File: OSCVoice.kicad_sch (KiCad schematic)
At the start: 39 parts, among them U10 TL072, U5 MCP6004, U6 4066, U8 4066, U9 SSI2131

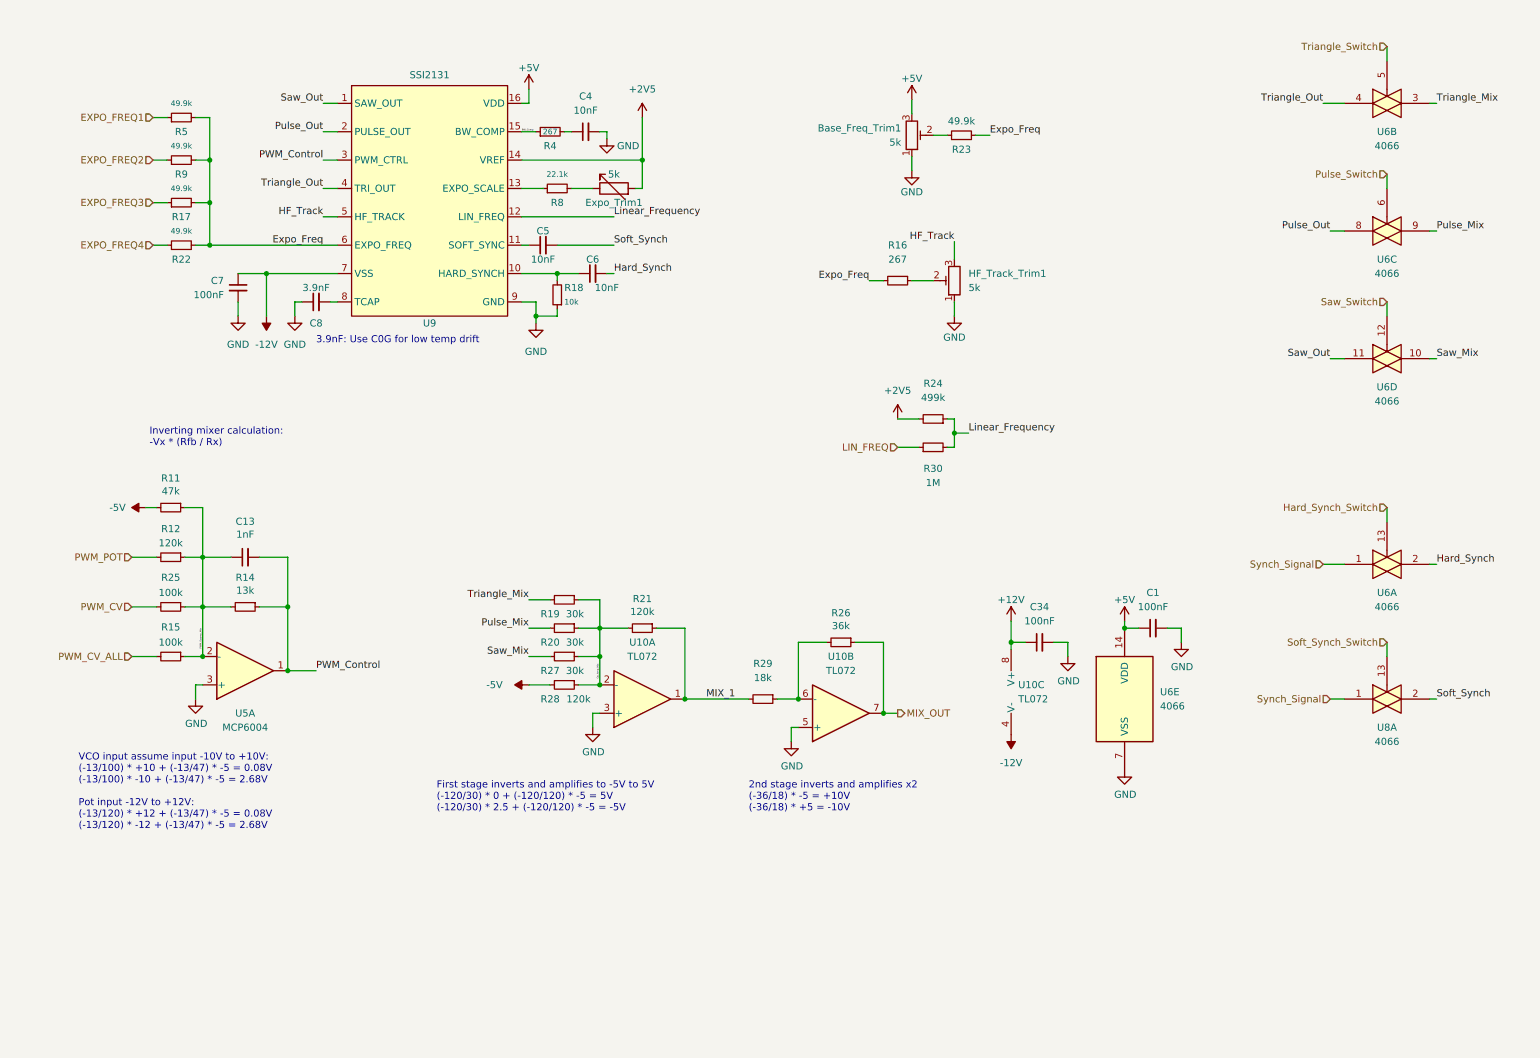
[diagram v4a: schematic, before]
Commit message: Duplicated layout of voices; power supply
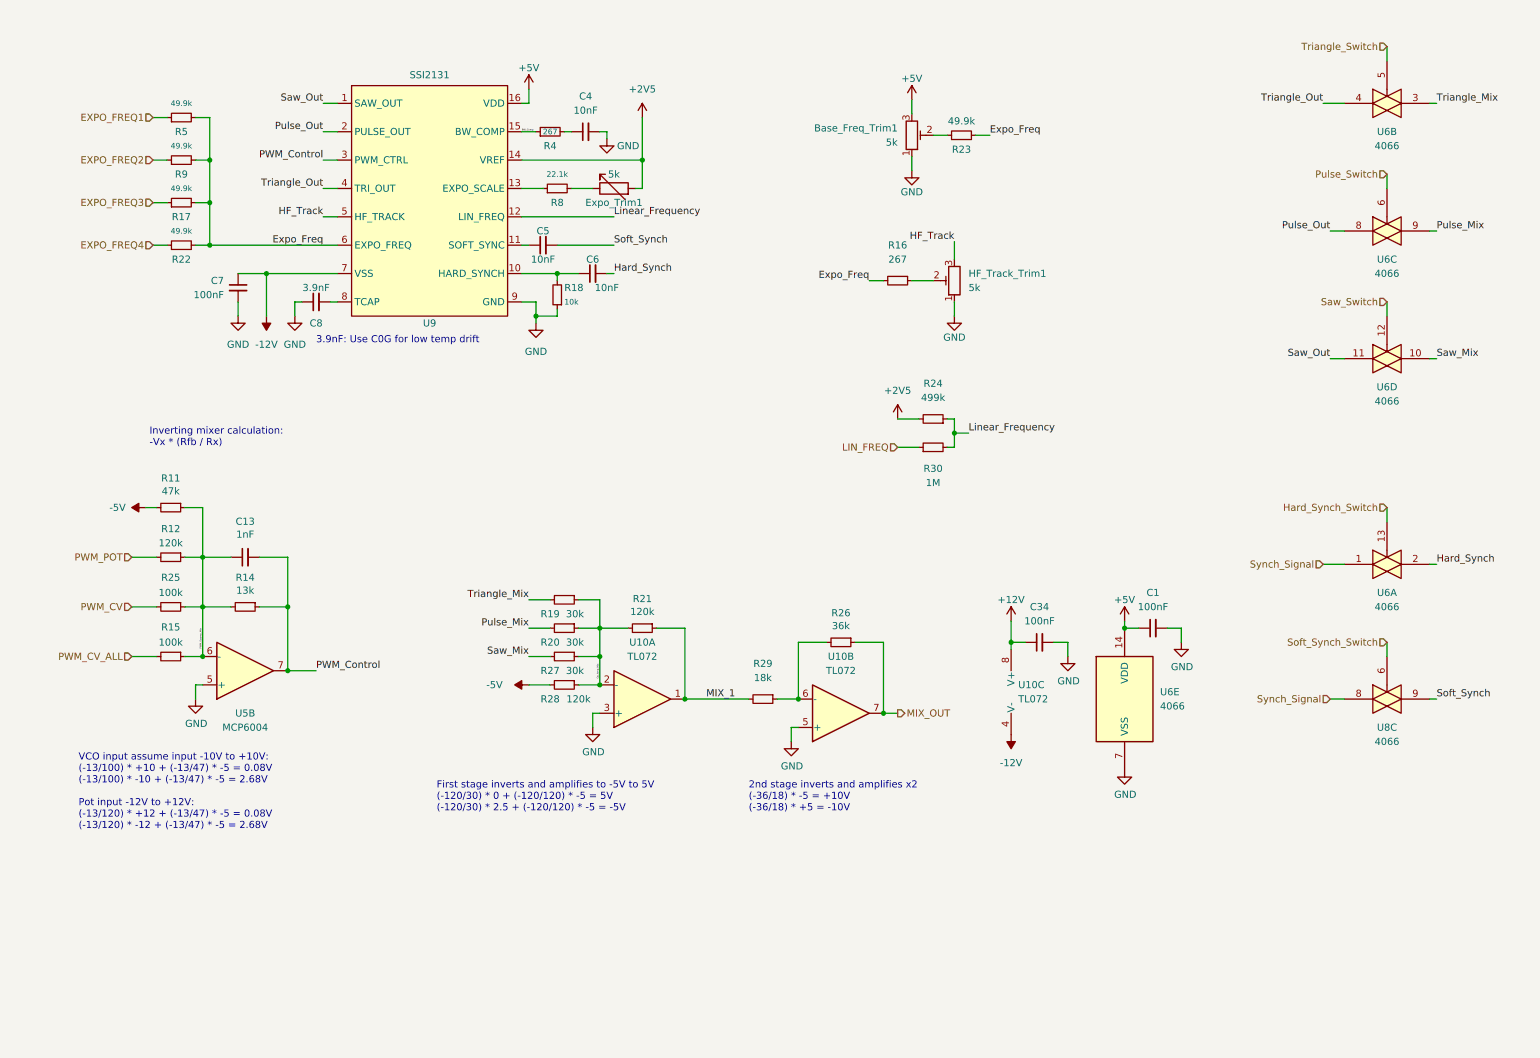
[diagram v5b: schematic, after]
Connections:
- net GND: now also U5.5 (+); no longer U5.3 (+)
- net PWM_Control: now also U5.7; no longer U5.1
- net PWM_Opamp_Mix: now also U5.6 (-); no longer U5.2 (-)
- net Soft_Synch: now also U8.9; no longer U8.2
- net Soft_Synch_Switch: now also U8.6; no longer U8.13
- net Synch_Signal: now also U8.8; no longer U8.1
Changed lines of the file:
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@@
     (pin "1")
   )
-  (symbol (lib_id "Amplifier_Operational:MCP6004") (at 54.61 130.81 0) (mirror x) (unit 1)
+  (symbol (lib_id "Amplifier_Operational:MCP6004") (at 54.61 130.81 0) (mirror x) (unit 2)
     (in_bom yes) (on_board yes) (fields_autoplaced)
     (property "Reference" "U5" (id 0) (at 54.61 138.43 0))
@@
     (pin "1")
   )
-  (symbol (lib_id "4xxx:4066") (at 259.08 135.89 0) (unit 1)
+  (symbol (lib_id "4xxx:4066") (at 259.08 135.89 0) (unit 3)
     (in_bom yes) (on_board yes) (fields_autoplaced)
     (property "Reference" "U8" (id 0) (at 259.08 140.97 0))
@@
   (symbol (lib_id "Device:R_Potentiometer_Trim") (at 173.99 34.925 0) (mirror x) (unit 1)
     (in_bom yes) (on_board yes) (fields_autoplaced)
-    (property "Reference" "Base_Freq_Trim1" (id 0) (at 172.085 33.6549 0)
+    (property "Reference" "Base_Freq_Trim1" (id 0) (at 171.45 33.6549 0)
       (effects (font (size 1.27 1.27)) (justify right))
     )
-    (property "Value" "5k" (id 1) (at 172.085 36.1949 0)
+    (property "Value" "5k" (id 1) (at 171.45 36.1949 0)
       (effects (font (size 1.27 1.27)) (justify right))
     )

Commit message: Routing power rails
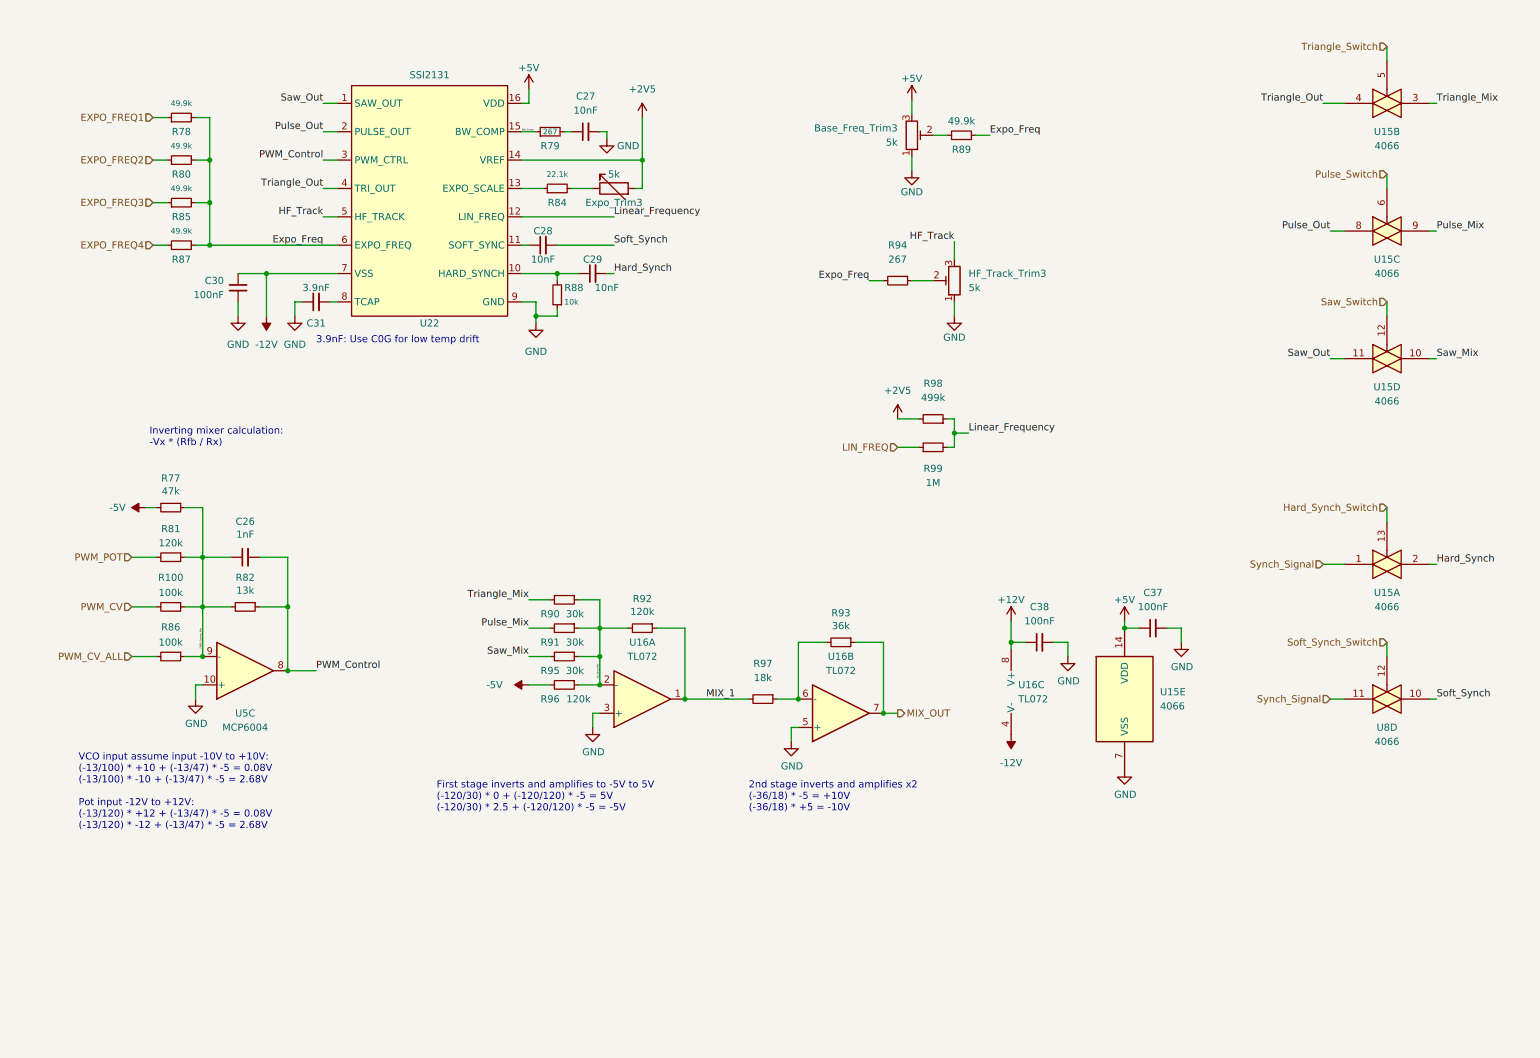
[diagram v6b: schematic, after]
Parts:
- renumbered Base_Freq_Trim1 to Base_Freq_Trim3, C13 to C26, C4 to C27, C5 to C28, C6 to C29, C7 to C30, C8 to C31, C1 to C37, C34 to C38, Expo_Trim1 to Expo_Trim3, HF_Track_Trim1 to HF_Track_Trim3, R25 to R100, R11 to R77, R5 to R78, R4 to R79, R9 to R80, R12 to R81, R14 to R82, R8 to R84, R17 to R85, R15 to R86, R22 to R87, R18 to R88, R23 to R89, R19 to R90, R20 to R91, R21 to R92, R26 to R93, R16 to R94, R27 to R95, R28 to R96, R29 to R97, R24 to R98, R30 to R99, U6 to U15, U10 to U16, U9 to U22
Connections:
- net GND: now also U5.10 (+); no longer U5.5 (+)
- net PWM_Control: now also U5.8; no longer U5.7
- net PWM_Opamp_Mix: now also U5.9 (-); no longer U5.6 (-)
- net Soft_Synch: now also U8.10; no longer U8.9
- net Soft_Synch_Switch: now also U8.12; no longer U8.6
- net Synch_Signal: now also U8.11; no longer U8.8

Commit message: Started control board schematic
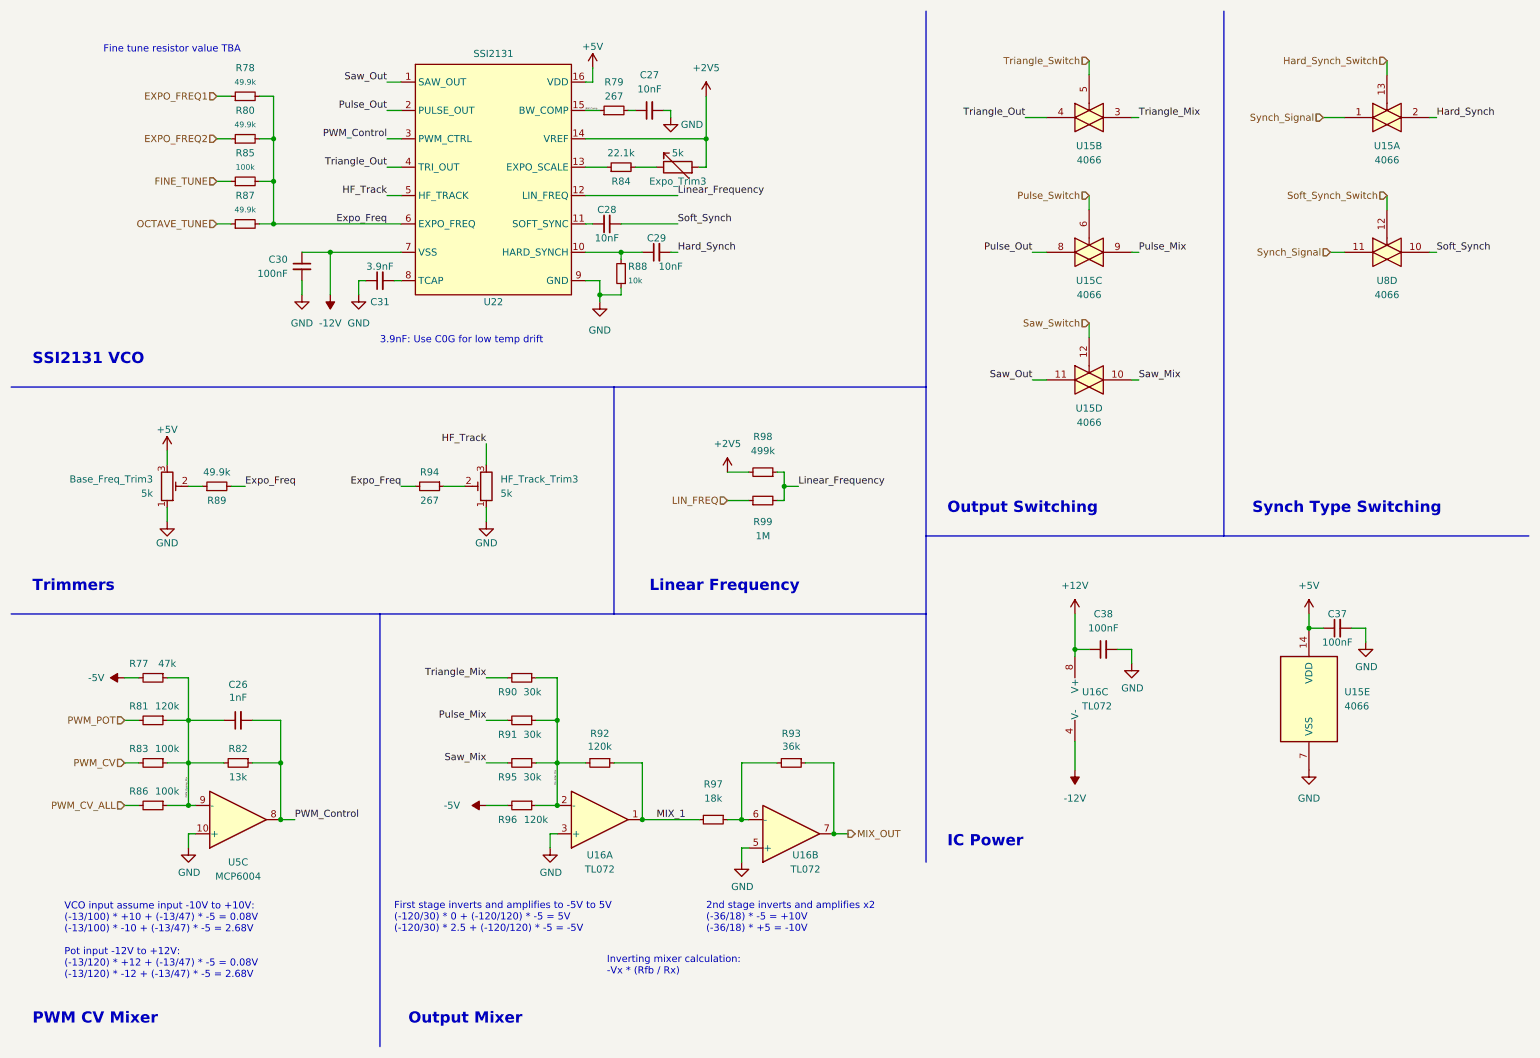
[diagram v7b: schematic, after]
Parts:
- R85: value 49.9k -> 100k
- renumbered R100 to R83
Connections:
- net EXPO_FREQ3 renamed FINE_TUNE
- net EXPO_FREQ4 renamed OCTAVE_TUNE
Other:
- note added: "Fine tune resistor value TBA"
- note added: "IC Power"
- note added: "Linear Frequency"
- note added: "Output Mixer"
- note added: "Output Switching"
- note added: "PWM CV Mixer"
- note added: "SSI2131 VCO"
- note added: "Synch Type Switching"
- note added: "Trimmers"
- company: (none) -> Mountjoy Modular
- title: (none) -> Quadraphone Voice
- moved on the sheet: Base_Freq_Trim3, C26, C27, C28, C29, C30, C31, C37, C38, Expo_Trim3, HF_Track_Trim3, R77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
